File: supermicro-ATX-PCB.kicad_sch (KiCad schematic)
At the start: 6 parts

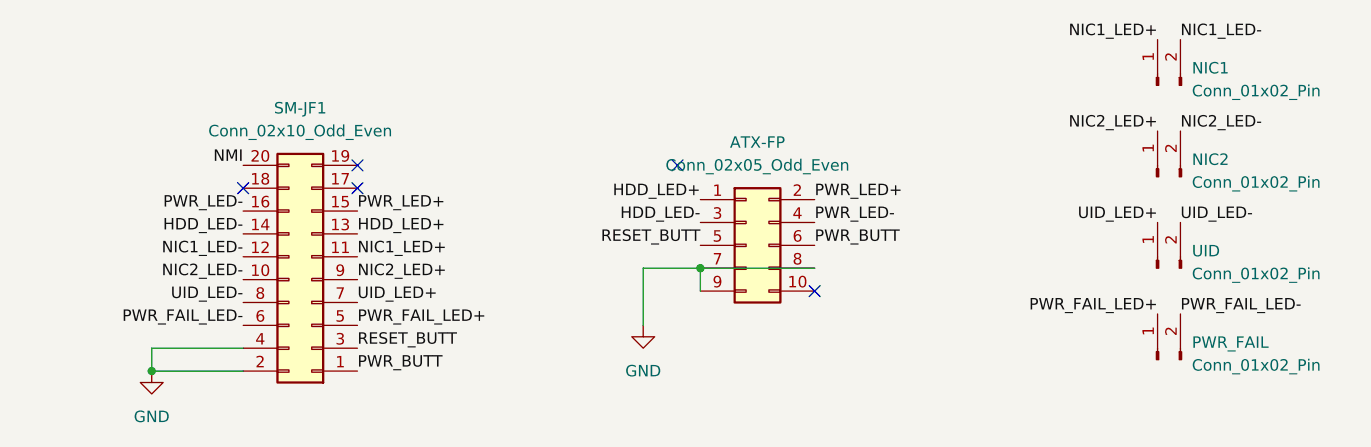
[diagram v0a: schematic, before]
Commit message: added through hole for female header
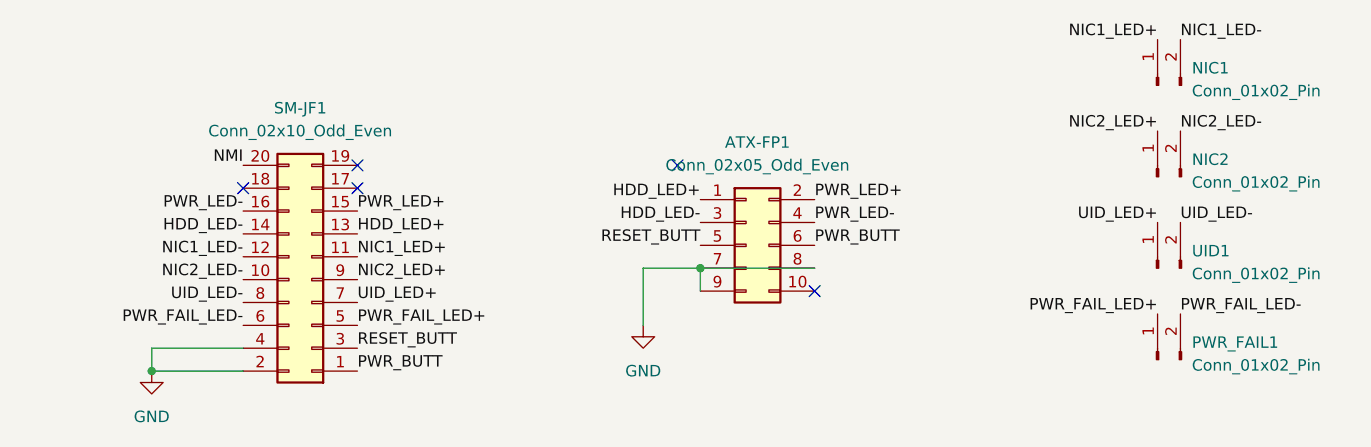
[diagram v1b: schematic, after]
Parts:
- renumbered ATX-FP to ATX-FP1, PWR_FAIL to PWR_FAIL1, UID to UID1
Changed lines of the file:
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@@
   (symbol (lib_id "Connector_Generic:Conn_02x05_Odd_Even") (at 133.35 46.99 0) (unit 1)
     (in_bom yes) (on_board yes) (dnp no) (fields_autoplaced)
-    (property "Reference" "ATX-FP" (at 134.62 35.56 0)
+    (property "Reference" "ATX-FP1" (at 134.62 35.56 0)
       (effects (font (size 1.27 1.27)))
     )
@@
       (project "supermicro-ATX-PCB"
         (path "/157eb82a-c702-4e17-b34a-5b8cd10c1865"
-          (reference "ATX-FP") (unit 1)
+          (reference "ATX-FP1") (unit 1)
         )
       )
@@
   (symbol (lib_id "Connector:Conn_01x02_Pin") (at 179.07 49.53 90) (unit 1)
     (in_bom yes) (on_board yes) (dnp no) (fields_autoplaced)
-    (property "Reference" "UID" (at 182.88 47.625 90)
+    (property "Reference" "UID1" (at 182.88 47.625 90)
       (effects (font (size 1.27 1.27)) (justify right))
     )
@@
       (project "supermicro-ATX-PCB"
         (path "/157eb82a-c702-4e17-b34a-5b8cd10c1865"
-          (reference "UID") (unit 1)
+          (reference "UID1") (unit 1)
         )
       )
@@
   (symbol (lib_id "Connector:Conn_01x02_Pin") (at 179.07 59.69 90) (unit 1)
     (in_bom yes) (on_board yes) (dnp no) (fields_autoplaced)
-    (property "Reference" "PWR_FAIL" (at 182.88 57.785 90)
+    (property "Reference" "PWR_FAIL1" (at 182.88 57.785 90)
       (effects (font (size 1.27 1.27)) (justify right))
     )
@@
       (project "supermicro-ATX-PCB"
         (path "/157eb82a-c702-4e17-b34a-5b8cd10c1865"
-          (reference "PWR_FAIL") (unit 1)
+          (reference "PWR_FAIL1") (unit 1)
         )
       )

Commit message: testing SMD Female
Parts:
- ATX-FP1: footprint Connector_PinSocket_2.54mm:PinSocket_2x05_P2.54mm_Vertical -> Connector_PinSocket_2.54mm:PinSocket_2x05_P2.54mm_Vertical_SMD
- renumbered PWR_FAIL1 to PWR_FAIL, UID1 to UID
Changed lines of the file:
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@@
       (effects (font (size 1.27 1.27)))
     )
-    (property "Footprint" "Connector_PinSocket_2.54mm:PinSocket_2x05_P2.54mm_Vertical" (at 133.35 46.99 0)
+    (property "Footprint" "Connector_PinSocket_2.54mm:PinSocket_2x05_P2.54mm_Vertical_SMD" (at 133.35 46.99 0)
       (effects (font (size 1.27 1.27)) hide)
     )
@@
   (symbol (lib_id "Connector:Conn_01x02_Pin") (at 179.07 49.53 90) (unit 1)
     (in_bom yes) (on_board yes) (dnp no) (fields_autoplaced)
-    (property "Reference" "UID1" (at 182.88 47.625 90)
+    (property "Reference" "UID" (at 182.88 47.625 90)
       (effects (font (size 1.27 1.27)) (justify right))
     )
@@
       (project "supermicro-ATX-PCB"
         (path "/157eb82a-c702-4e17-b34a-5b8cd10c1865"
-          (reference "UID1") (unit 1)
+          (reference "UID") (unit 1)
         )
       )
@@
   (symbol (lib_id "Connector:Conn_01x02_Pin") (at 179.07 59.69 90) (unit 1)
     (in_bom yes) (on_board yes) (dnp no) (fields_autoplaced)
-    (property "Reference" "PWR_FAIL1" (at 182.88 57.785 90)
+    (property "Reference" "PWR_FAIL" (at 182.88 57.785 90)
       (effects (font (size 1.27 1.27)) (justify right))
     )
@@
       (project "supermicro-ATX-PCB"
         (path "/157eb82a-c702-4e17-b34a-5b8cd10c1865"
-          (reference "PWR_FAIL1") (unit 1)
+          (reference "PWR_FAIL") (unit 1)
         )
       )

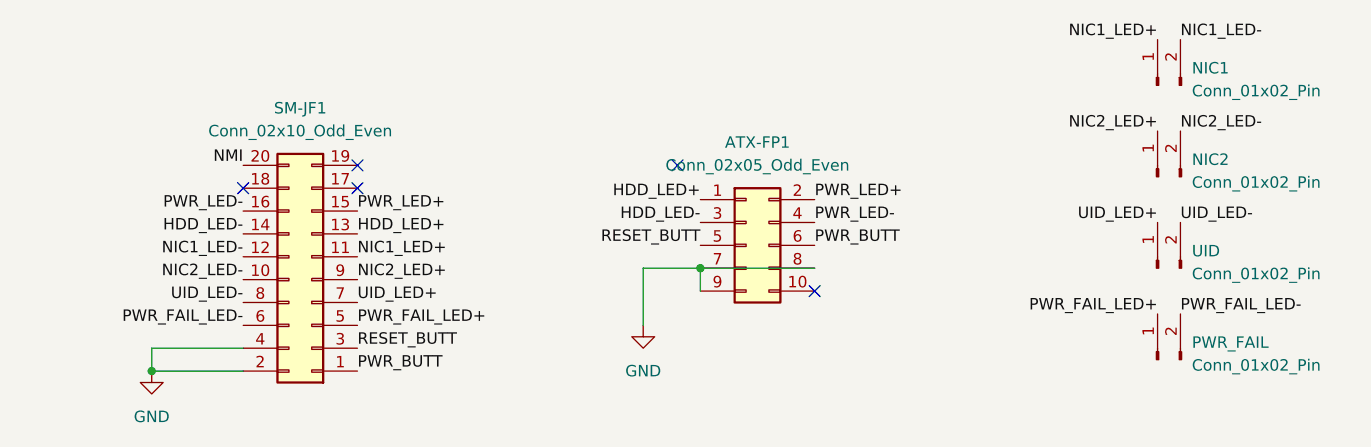
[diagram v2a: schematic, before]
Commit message: switched polarity of LEDs, isolated all terminals of buttons
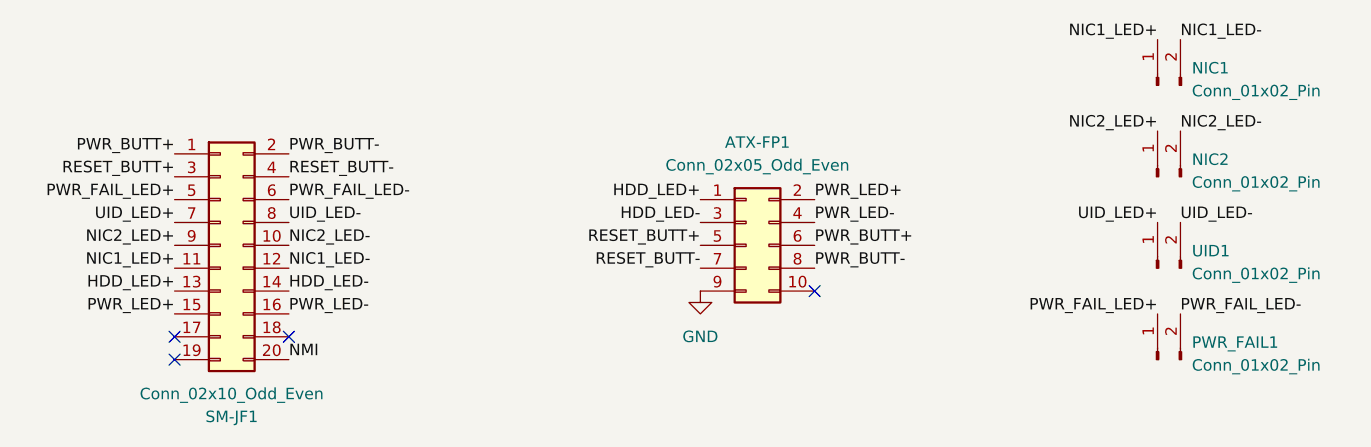
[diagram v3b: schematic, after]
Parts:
- ATX-FP1: footprint Connector_PinSocket_2.54mm:PinSocket_2x05_P2.54mm_Vertical_SMD -> Connector_PinSocket_2.54mm:PinSocket_2x05_P2.54mm_Vertical
- SM-JF1: footprint Connector_PinSocket_2.54mm:PinSocket_2x10_P2.54mm_Vertical -> Connector_PinHeader_2.54mm:PinHeader_2x10_P2.54mm_Vertical
- renumbered PWR_FAIL to PWR_FAIL1, UID to UID1
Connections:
- net GND: no longer ATX-FP1.7 (Pin_7), ATX-FP1.8 (Pin_8), SM-JF1.2 (Pin_2), SM-JF1.4 (Pin_4)
- net PWR_BUTT renamed PWR_BUTT+
- net RESET_BUTT renamed RESET_BUTT+
- new net PWR_BUTT-: ATX-FP1.8 (Pin_8), SM-JF1.2 (Pin_2)
- new net RESET_BUTT-: ATX-FP1.7 (Pin_7), SM-JF1.4 (Pin_4)
- no-connect marks 5 -> 4
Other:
- moved on the sheet: SM-JF1
